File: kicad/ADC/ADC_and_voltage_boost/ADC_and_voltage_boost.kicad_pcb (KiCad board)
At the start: 2 copper layers, 29.7 x 43.4 mm, 12 parts, among them J1 Screw_Terminal_01x04, J2 Screw_Terminal_01x04, U3 MOUDLE-SEEEDUINO-XIAO-ESP32C3, U4 MAX1032BEUG_

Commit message: added ino file
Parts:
- added REF**: TerminalBlock_Xinya_XY308-2.54-2P_1x02_P2.54mm_Horizontal, TerminalBlock:TerminalBlock_Xinya_XY308-2.54-2P_1x02_P2.54mm_Horizontal, F.Cu at (135.1, 114.3)
- moved REF** 41.4 mm to (160.5, 128.0)
- moved REF** 3.14 mm to (136.1, 86.1)
- moved J1 2.30 mm to (136.4, 91.9)
- moved J2 1.40 mm to (155.6, 87.5)
- moved C9 1.36 mm to (157.0, 96.3)
- moved C2 1.11 mm to (156.7, 98.3)
- moved C8 1.05 mm to (156.7, 94.2)
- moved C11 0.51 mm to (143.5, 95.0)
- moved C1 0.44 mm to (143.6, 93.0)
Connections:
- U3 pad 16: (no net) -> +3.3V
- U3 pad 17: (no net) -> GND
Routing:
- net GND: track 75.1 -> 161.4 mm, vias 2 -> 3
- net +5V: track 32.8 -> 62.7 mm
- net +3.3V: track 88.2 -> 116.6 mm
- net (no net): track 20.2 -> 0.00 mm, vias 4 -> 0
- net Net-(J2-Pin_3): track 7.55 -> 9.00 mm
- net Net-(U4-REF): track 2.74 -> 4.10 mm
- net Net-(U4-REFCAP): track 2.29 -> 3.41 mm
- net Net-(J2-Pin_1): track 11.3 -> 12.0 mm
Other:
- board size 29.7 x 43.4 mm -> 32.5 x 49 mm
- board text removed: "Screw_Terminal_01x04"

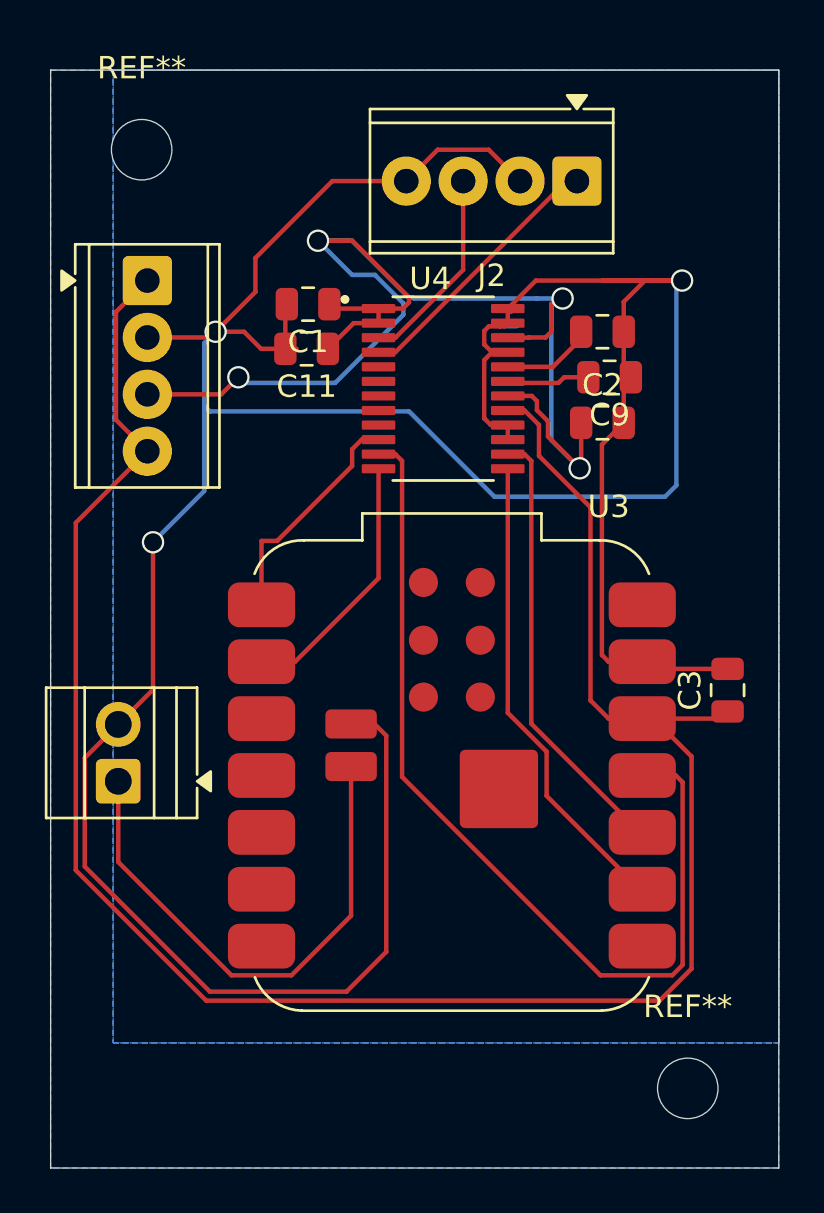
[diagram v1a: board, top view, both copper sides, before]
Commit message: finished ADC
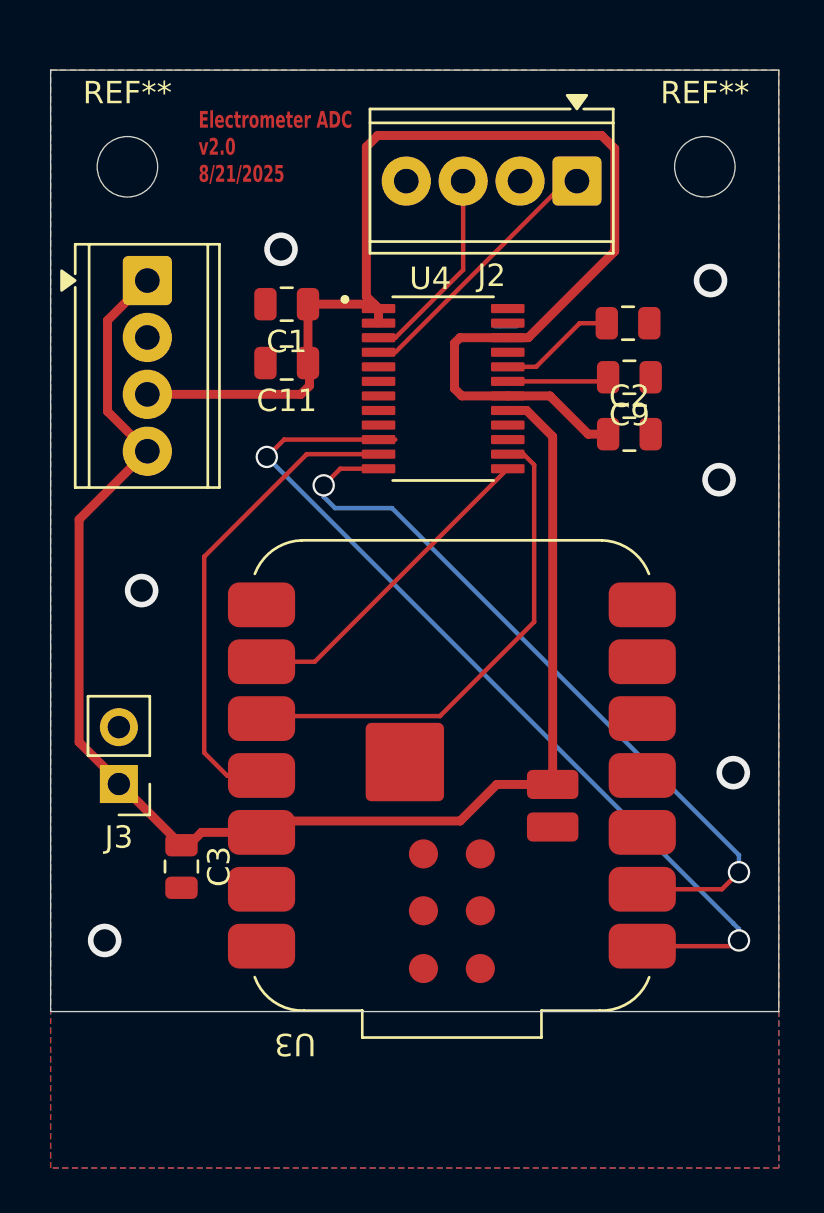
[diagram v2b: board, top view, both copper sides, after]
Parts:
- removed the REF** at (136.1, 86.1)
- removed the REF** at (135.1, 114.3)
- removed the REF** at (160.5, 128.0)
- added J3: Screw_Terminal_01x02, Connector_PinHeader_2.54mm:PinHeader_1x02_P2.54mm_Vertical, F.Cu at (135.1, 114.4)
- added REF**: MountingHole_2.7mm_M2.5_DIN965, MountingHole:MountingHole_2.7mm_M2.5_DIN965, F.Cu at (135.5, 86.9)
- added REF**: MountingHole_2.7mm_M2.5_DIN965, MountingHole:MountingHole_2.7mm_M2.5_DIN965, F.Cu at (161.3, 86.9)
- C1, C11, C2, C3, C9: value 0.1e-6 -> 100n
- C8: value 1e-6 -> 1u
- moved C3 25.6 mm to (137.9, 118.1), turned to -90 degrees
- moved C2 1.31 mm to (157.9, 98.8)
- moved C8 1.20 mm to (157.9, 93.9)
- moved C11 1.09 mm to (142.6, 95.6)
- moved C1 0.95 mm to (142.6, 93.0)
- moved C9 0.88 mm to (157.9, 96.3)
- turned U3 to 180 degrees
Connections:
- net +3.3V renamed +BATT
- net Net-(U3-PA02_A0_D0) renamed /~{CS}
- net Net-(U3-PA5_A9_D9_MISO) renamed /MISO
- net Net-(U3-PA6_A10_D10_MOSI) renamed /MOSI
- net Net-(U3-PA7_A8_D8_SCK) renamed /SCK
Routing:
- net GND: track 161.4 -> 1.02 mm, vias 3 -> 6
- net +BATT: track 116.6 -> 65.6 mm
- net /~{CS}: track 10.5 -> 40.8 mm, vias 0 -> 2
- net Net-(U3-PA4_A1_D1): track 11.7 -> 33.8 mm, vias 0 -> 2
- net /MOSI: track 41.8 -> 21.4 mm
- net /SCK: track 22.1 -> 14.6 mm
- net +5V: track 62.7 -> 57.1 mm, vias 4 -> 0
- net /MISO: track 19.9 -> 22.4 mm
- net Net-(U4-REFCAP): track 3.41 -> 4.56 mm
- net Net-(U4-REF): track 4.10 -> 5.23 mm
- added copper zone on F.Cu, net GND
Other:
- board size 32.5 x 49 mm -> 32.5 x 42 mm
- board text added: "Electrometer ADC v2.0 8/21/2025"

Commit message: committing some adc board changes
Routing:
- net GND: track 1.02 -> 54.9 mm, vias 6 -> 7
